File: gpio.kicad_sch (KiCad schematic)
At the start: 0 parts

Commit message: */*: change lib id to CHIPSAlliance
Signed-off-by: Huang Rui <vowstar@gmail.com>
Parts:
- added U4: SN74LVC1T45DBV, Package_TO_SOT_SMD:SOT-23-6, symbol Logic_LevelTranslator:SN74LVC1T45DBV
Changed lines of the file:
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@@
 (kicad_sch (version 20230121) (generator eeschema)
   (paper "A4")
+  (symbol (lib_id "Logic_LevelTranslator:SN74LVC1T45DBV") (at 109.22 86.36 0) (unit 1)
+    (in_bom yes) (on_board yes) (dnp no)
+    (property "Reference" "U4" (at 102.87 95.25 0)
+      (effects (font (size 1.27 1.27)))
+    )
+    (property "Value" "SN74LVC1T45DBV" (at 119.38 95.25 0)
+      (effects (font (size 1.27 1.27)))
+    )
+    (property "Footprint" "Package_TO_SOT_SMD:SOT-23-6" (at 109.22 97.79 0)
+      (effects (font (size 1.27 1.27)) hide)
+    )
+    (property "Datasheet" "http://www.ti.com/lit/ds/symlink/sn74lvc1t45.pdf" (at 86.36 102.87 0)
+      (effects (font (size 1.27 1.27)) hide)
+    )
+    (pin "1")
+    (pin "2")
+    (pin "3")
+    (pin "4")
+    (pin "5")
+    (pin "6")
+    (instances
+      (project "fmc_usb_gpio_spi_jtag"
+        (path "/387bfcf1-ae49-4b85-be89-3bb02ce2e960/4ff80468-3372-4da6-9aa6-0708696df1f4"
+          (reference "U4") (unit 1)
+        )
+        (path "/387bfcf1-ae49-4b85-be89-3bb02ce2e960/8f11314c-d9eb-415d-8d76-07f3be42979a"
+          (reference "U4") (unit 1)
+        )
+      )
+    )
+  )
 )

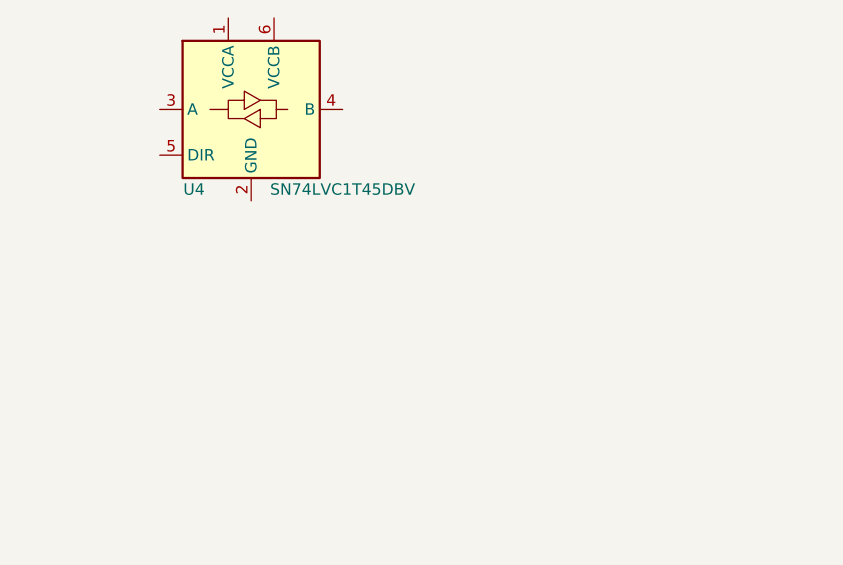
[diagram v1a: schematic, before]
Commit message: gpio.kicad_sch: add PMOD Conn_02x06_Odd_Even
Signed-off-by: Huang Rui <vowstar@gmail.com>
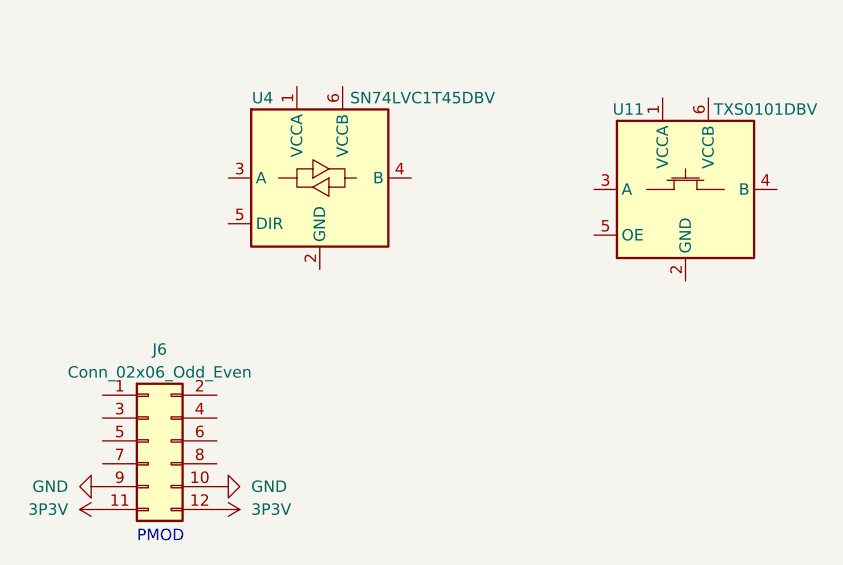
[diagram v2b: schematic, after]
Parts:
- added J6: Conn_02x06_Odd_Even, symbol Connector_Generic:Conn_02x06_Odd_Even
- added U11: TXS0101DBV, Package_TO_SOT_SMD:SOT-23-6, symbol CHIPSAlliance_Logic:TXS0101DBV
- U4: symbol Logic_LevelTranslator:SN74LVC1T45DBV -> CHIPSAlliance_Logic:SN74LVC1T45DBV; JLCPCB Rotation Offset (none) -> -180
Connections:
- new net GND: J6.10 (Pin_10), J6.9 (Pin_9)
- new net P3V3: J6.11 (Pin_11), J6.12 (Pin_12)
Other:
- note added: "PMOD"
- moved on the sheet: U4
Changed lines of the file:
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@@
 (kicad_sch (version 20230121) (generator eeschema)
   (paper "A4")
-  (symbol (lib_id "Logic_LevelTranslator:SN74LVC1T45DBV") (at 109.22 86.36 0) (unit 1)
-    (in_bom yes) (on_board yes) (dnp no)
-    (property "Reference" "U4" (at 102.87 95.25 0)
+  (text "PMOD" (at 96.52 134.62 0)
+    (effects (font (size 1.27 1.27)) (justify left bottom))
+  )
+  (symbol (lib_id "Connector_Generic:Conn_02x06_Odd_Even") (at 97.79 123.19 0) (unit 1)
+    (in_bom yes) (on_board yes) (dnp no) (fields_autoplaced)
+    (property "Reference" "J6" (at 99.06 113.03 0)
       (effects (font (size 1.27 1.27)))
     )
-    (property "Value" "SN74LVC1T45DBV" (at 119.38 95.25 0)
+    (property "Value" "Conn_02x06_Odd_Even" (at 99.06 115.57 0)
+      (effects (font (size 1.27 1.27)))
+    )
+    (property "Footprint" "" (at 97.79 123.19 0)
+      (effects (font (size 1.27 1.27)) hide)
+    )
+    (property "Datasheet" "~" (at 97.79 123.19 0)
+      (effects (font (size 1.27 1.27)) hide)
+    )
+    (pin "1")
+    (pin "10")
+    (pin "11")
+    (pin "12")
+    (pin "2")
+    (pin "3")
+    (pin "4")
+    (pin "5")
+    (pin "6")
+    (pin "7")
+    (pin "8")
+    (pin "9")
+    (instances
+      (project "fmc_usb_gpio_spi_jtag"
+        (path "/387bfcf1-ae49-4b85-be89-3bb02ce2e960/9cd800a1-5b4a-4dab-b708-f8f78f4f7813"
+          (reference "J6") (unit 1)
+        )
+        (path "/387bfcf1-ae49-4b85-be89-3bb02ce2e960/8f11314c-d9eb-415d-8d76-07f3be42979a"
+          (reference "J6") (unit 1)
+        )
+      )
+    )
+  )
+  (symbol (lib_id "CHIPSAlliance_Logic:TXS0101DBV") (at 149.86 87.63 0) (unit 1)
+    (in_bom yes) (on_board yes) (dnp no)
+    (property "Reference" "U11" (at 151.13 86.36 0)
+      (effects (font (size 1.27 1.27)))
+    )
+    (property "Value" "TXS0101DBV" (at 166.37 86.36 0)
+      (effects (font (size 1.27 1.27)))
+    )
+    (property "Footprint" "Package_TO_SOT_SMD:SOT-23-6" (at 151.13 99.06 0)
+      (effects (font (size 1.27 1.27)) (justify left) hide)
+    )
+    (property "Datasheet" "https://www.ti.com/lit/ds/symlink/txs0101.pdf" (at 149.86 111.76 0)
+      (effects (font (size 1.27 1.27)) hide)
+    )
+    (property "JLCPCB Rotation Offset" "-180" (at 149.86 111.76 0)
+      (effects (font (size 1.27 1.27)) (justify left) hide)
+    )
+    (pin "1")
+    (pin "2")
+    (pin "3")
+    (pin "4")
+    (pin "5")
+    (pin "6")
+    (instances
+      (project "fmc_usb_gpio_spi_jtag"
+        (path "/387bfcf1-ae49-4b85-be89-3bb02ce2e960/050a965f-1566-4fd5-8eeb-6ab96a9baeba"
+          (reference "U11") (unit 1)
+        )
+        (path "/387bfcf1-ae49-4b85-be89-3bb02ce2e960/8f11314c-d9eb-415d-8d76-07f3be42979a"
+          (reference "U11") (unit 1)
+        )
+      )
+    )
+  )
+  (symbol (lib_id "power:GND") (at 105.41 128.27 90) (unit 1)
+    (in_bom yes) (on_board yes) (dnp no)
+    (property "Reference" "#PWR074" (at 111.76 128.27 0)
+      (effects (font (size 1.27 1.27)) hide)
+    )
+    (property "Value" "GND" (at 109.22 128.27 90)
+      (effects (font (size 1.27 1.27)) (justify right))
+    )
+    (property "Footprint" "" (at 105.41 128.27 0)
+      (effects (font (size 1.524 1.524)))
+    )
+    (property "Datasheet" "" (at 105.41 128.27 0)
+      (effects (font (size 1.524 1.524)))
+    )
+    (pin "1")
+    (instances
+      (project "fmc_usb_gpio_spi_jtag"
+        (path "/387bfcf1-ae49-4b85-be89-3bb02ce2e960/4338fda8-0ea2-4bf2-b1c2-c685ef11d6a0"
+          (reference "#PWR074") (unit 1)
+        )
+        (path "/387bfcf1-ae49-4b85-be89-3bb02ce2e960/8f11314c-d9eb-415d-8d76-07f3be42979a"
+          (reference "#PWR0172") (unit 1)
+        )
+      )
+    )
+  )
+  (symbol (lib_id "power:VDD") (at 92.71 130.81 90) (unit 1)
+    (in_bom yes) (on_board yes) (dnp no)
+    (property "Reference" "#PWR073" (at 96.52 130.81 0)
+      (effects (font (size 1.27 1.27)) hide)
+    )
+    (property "Value" "3P3V" (at 88.9 130.81 90)
+      (effects (font (size 1.27 1.27)) (justify left))
+    )
+    (property "Footprint" "" (at 92.71 130.81 0)
+      (effects (font (size 1.524 1.524)))
+    )
+    (property "Datasheet" "" (at 92.71 130.81 0)
+      (effects (font (size 1.524 1.524)))
+    )
+    (pin "1")
+    (instances
+      (project "fmc_usb_gpio_spi_jtag"
+        (path "/387bfcf1-ae49-4b85-be89-3bb02ce2e960/4338fda8-0ea2-4bf2-b1c2-c685ef11d6a0"
+          (reference "#PWR073") (unit 1)
+        )
+        (path "/387bfcf1-ae49-4b85-be89-3bb02ce2e960/8f11314c-d9eb-415d-8d76-07f3be42979a"
+          (reference "#PWR0171") (unit 1)
+        )
+      )
+    )
+  )
+  (symbol (lib_id "power:GND") (at 92.71 128.27 270) (unit 1)
+    (in_bom yes) (on_board yes) (dnp no)
+    (property "Reference" "#PWR072" (at 86.36 128.27 0)
+      (effects (font (size 1.27 1.27)) hide)
+    )
+    (property "Value" "GND" (at 88.9 128.27 90)
+      (effects (font (size 1.27 1.27)) (justify right))
+    )
+    (property "Footprint" "" (at 92.71 128.27 0)
+      (effects (font (size 1.524 1.524)))
+    )
+    (property "Datasheet" "" (at 92.71 128.27 0)
+      (effects (font (size 1.524 1.524)))
+    )
+    (pin "1")
+    (instances
+      (project "fmc_usb_gpio_spi_jtag"
+        (path "/387bfcf1-ae49-4b85-be89-3bb02ce2e960/4338fda8-0ea2-4bf2-b1c2-c685ef11d6a0"
+          (reference "#PWR072") (unit 1)
+        )
+        (path "/387bfcf1-ae49-4b85-be89-3bb02ce2e960/8f11314c-d9eb-415d-8d76-07f3be42979a"
+          (reference "#PWR0170") (unit 1)
+        )
+      )
+    )
+  )
+  (symbol (lib_id "power:VDD") (at 105.41 130.81 270) (unit 1)
+    (in_bom yes) (on_board yes) (dnp no)
+    (property "Reference" "#PWR073" (at 101.6 130.81 0)
+      (effects (font (size 1.27 1.27)) hide)
+    )
+    (property "Value" "3P3V" (at 109.22 130.81 90)
+      (effects (font (size 1.27 1.27)) (justify left))
+    )
+    (property "Footprint" "" (at 105.41 130.81 0)
+      (effects (font (size 1.524 1.524)))
+    )
+    (property "Datasheet" "" (at 105.41 130.81 0)
+      (effects (font (size 1.524 1.524)))
+    )
+    (pin "1")
+    (instances
+      (project "fmc_usb_gpio_spi_jtag"
+        (path "/387bfcf1-ae49-4b85-be89-3bb02ce2e960/4338fda8-0ea2-4bf2-b1c2-c685ef11d6a0"
+          (reference "#PWR073") (unit 1)
+        )
+        (path "/387bfcf1-ae49-4b85-be89-3bb02ce2e960/8f11314c-d9eb-415d-8d76-07f3be42979a"
+          (reference "#PWR0174") (unit 1)
+        )
+      )
+    )
+  )
+  (symbol (lib_id "CHIPSAlliance_Logic:SN74LVC1T45DBV") (at 109.22 86.36 0) (unit 1)
+    (in_bom yes) (on_board yes) (dnp no)
+    (property "Reference" "U4" (at 110.49 85.09 0)
+      (effects (font (size 1.27 1.27)))
+    )
+    (property "Value" "SN74LVC1T45DBV" (at 128.27 85.09 0)
       (effects (font (size 1.27 1.27)))
     )
@@
       (effects (font (size 1.27 1.27)) hide)
     )
+    (property "JLCPCB Rotation Offset" "-180" (at 109.22 110.49 0)
+      (effects (font (size 1.27 1.27)) (justify left) hide)
+    )
     (pin "1")

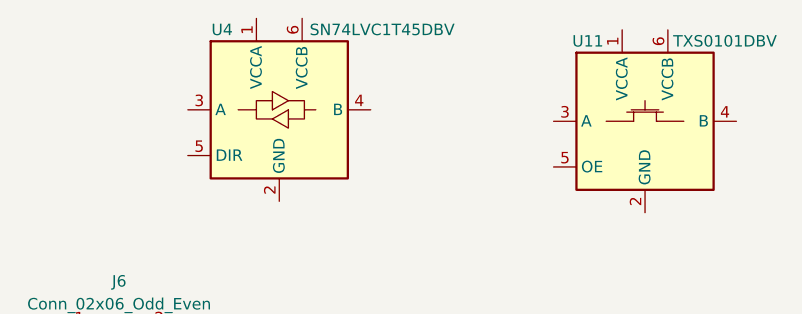
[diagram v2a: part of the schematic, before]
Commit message: *.kicad_sch: changed SN74LVC1T45DBV to symbol AIP74LVC1T45GB236TR
Signed-off-by: Huang Rui <vowstar@gmail.com>
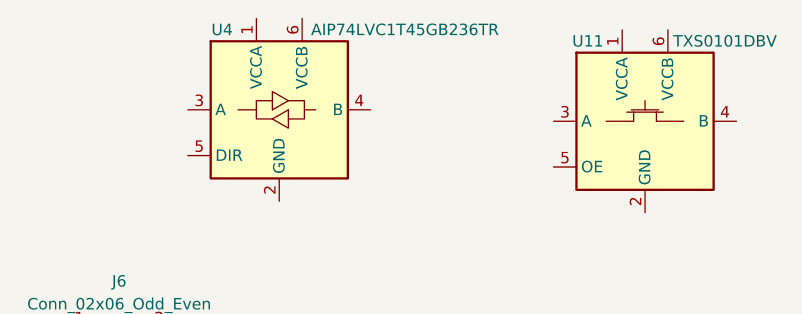
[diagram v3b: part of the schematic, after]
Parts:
- U4: value SN74LVC1T45DBV -> AIP74LVC1T45GB236TR; symbol CHIPSAlliance_Logic:SN74LVC1T45DBV -> CHIPSAlliance_Logic:AIP74LVC1T45GB236TR
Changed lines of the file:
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@@
     )
   )
-  (symbol (lib_id "CHIPSAlliance_Logic:SN74LVC1T45DBV") (at 109.22 86.36 0) (unit 1)
+  (symbol (lib_id "CHIPSAlliance_Logic:AIP74LVC1T45GB236TR") (at 109.22 86.36 0) (unit 1)
     (in_bom yes) (on_board yes) (dnp no)
     (property "Reference" "U4" (at 110.49 85.09 0)
       (effects (font (size 1.27 1.27)))
     )
-    (property "Value" "SN74LVC1T45DBV" (at 128.27 85.09 0)
+    (property "Value" "AIP74LVC1T45GB236TR" (at 130.81 85.09 0)
       (effects (font (size 1.27 1.27)))
     )
     (property "Footprint" "Package_TO_SOT_SMD:SOT-23-6" (at 109.22 97.79 0)
-      (effects (font (size 1.27 1.27)) hide)
+      (effects (font (size 1.27 1.27)) (justify left) hide)
     )
-    (property "Datasheet" "http://www.ti.com/lit/ds/symlink/sn74lvc1t45.pdf" (at 86.36 102.87 0)
-      (effects (font (size 1.27 1.27)) hide)
+    (property "Datasheet" "https://atta.szlcsc.com/upload/public/pdf/source/20220915/C3F384B245F14B1C45E49B7D1719C9B2.pdf" (at 86.36 102.87 0)
+      (effects (font (size 1.27 1.27)) (justify left) hide)
     )
     (property "JLCPCB Rotation Offset" "-180" (at 109.22 110.49 0)
